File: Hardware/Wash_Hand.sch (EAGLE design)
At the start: 86 parts, among them IC1 LM358D, IC2 LP298XS, IC3 405016TSSOP, J1 I2C, J2 ICSP, J3 SPI, J4 9V_CONN, J5 EXT_VCC, J6 6_PIN_SERIAL_CABLEPTH, Q1 16.0 Mhz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

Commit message: Board/Schematic: CH340G; V3 goes to GND with 4.7-20nF..
while we also had VCC connected to it. That is the
datasheet says: "When using 5V operation, supply 5V
to VCC pin, and decouple the internal 3.3V reference with
a capacitor of 4.7-20nF from _V3 pin to ground_.

We had the VCC being hooked up to the capacitor..

Signed-off-by: Konrad Rzeszutek Wilk <konrad@kernel.org>
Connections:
- new net N$17: C14.1, JP6.1
- net VCC: no longer C14.1, JP6.1
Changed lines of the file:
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@@
 <label x="119.38" y="86.36" size="1.778" layer="95" rot="R180" xref="yes"/>
-</segment>
-<segment>
-<pinref part="C14" gate="G$1" pin="1"/>
-<wire x1="45.72" y1="96.52" x2="35.56" y2="96.52" width="0.1524" layer="91"/>
-<label x="35.56" y="96.52" size="1.778" layer="95" rot="R180" xref="yes"/>
-<pinref part="JP6" gate="G$1" pin="1"/>
-<wire x1="45.72" y1="96.52" x2="45.72" y2="99.06" width="0.1524" layer="91"/>
-<junction x="45.72" y="96.52"/>
 </segment>
 </net>
@@
 </segment>
 <segment>
+<pinref part="C16" gate="G$1" pin="1"/>
+<pinref part="X_36" gate="G$1" pin="0"/>
+<wire x1="121.92" y1="167.64" x2="121.92" y2="172.72" width="0.1524" layer="91"/>
+</segment>
+<segment>
 <pinref part="X_34" gate="G$1" pin="0"/>
 <pinref part="C14" gate="G$1" pin="2"/>
 <wire x1="45.72" y1="83.82" x2="45.72" y2="88.9" width="0.1524" layer="91"/>
-</segment>
-<segment>
-<pinref part="C16" gate="G$1" pin="1"/>
-<pinref part="X_36" gate="G$1" pin="0"/>
-<wire x1="121.92" y1="167.64" x2="121.92" y2="172.72" width="0.1524" layer="91"/>
 </segment>
 </net>
@@
 </segment>
 </net>
+<net name="N$17" class="0">
+<segment>
+<pinref part="C14" gate="G$1" pin="1"/>
+<pinref part="JP6" gate="G$1" pin="1"/>
+<wire x1="45.72" y1="96.52" x2="45.72" y2="99.06" width="0.1524" layer="91"/>
+</segment>
+</net>

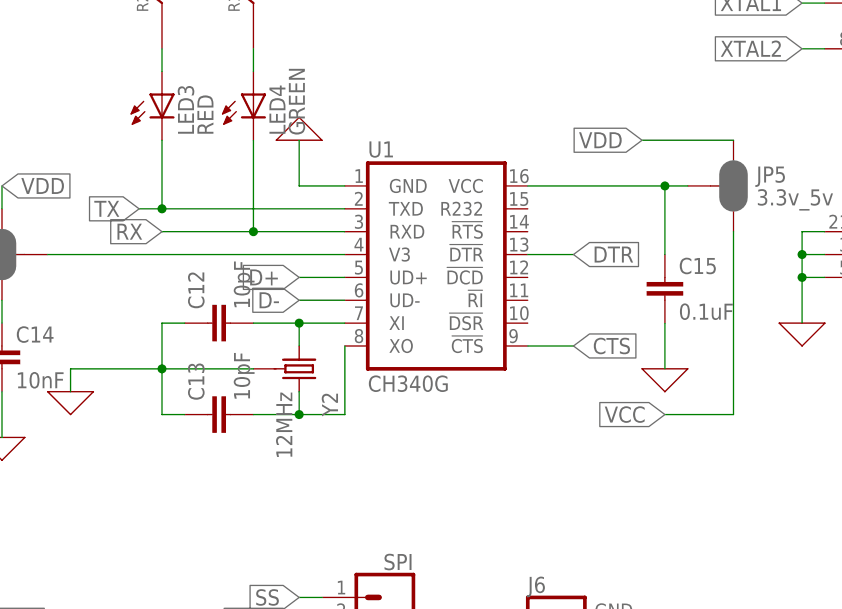
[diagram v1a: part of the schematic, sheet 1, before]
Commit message: Board/Schematic: Name the nets on the CH340G/Adjust location of GREEN,RED,CH340G
.. to make it easier to trace and diagnose.

Signed-off-by: Konrad Rzeszutek Wilk <konrad@kernel.org>
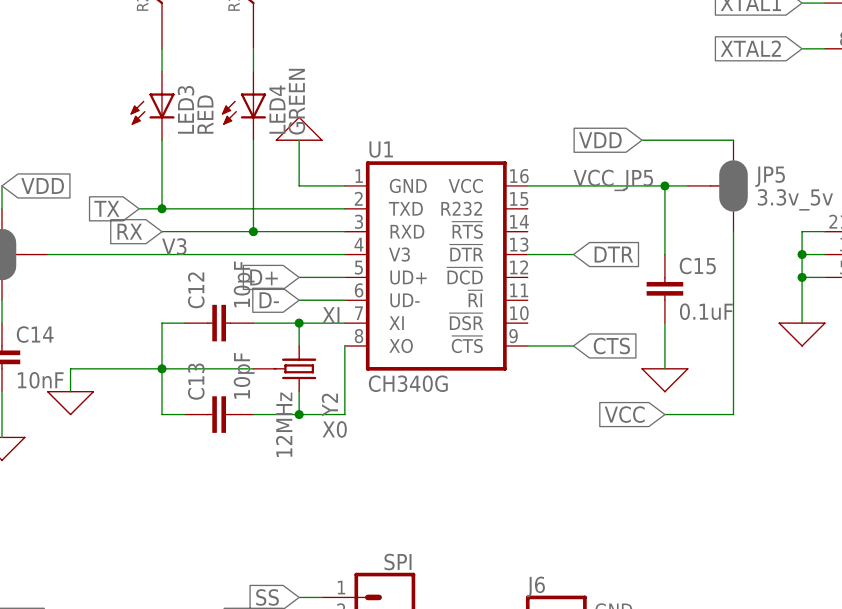
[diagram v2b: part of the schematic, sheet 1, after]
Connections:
- net N$1 renamed XI
- net N$19 renamed VCC_JP5
- net N$21 renamed X0
- net N$9 renamed V3
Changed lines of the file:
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@@
 </segment>
 </net>
-<net name="N$21" class="0">
+<net name="X0" class="0">
 <segment>
 <pinref part="U1" gate="U1" pin="XO"/>
@@
 <wire x1="73.66" y1="86.36" x2="78.74" y2="86.36" width="0.1524" layer="91"/>
 <junction x="78.74" y="86.36"/>
+<label x="81.28" y="83.82" size="1.778" layer="95"/>
 </segment>
 </net>
@@
 </segment>
 </net>
-<net name="N$1" class="0">
+<net name="XI" class="0">
 <segment>
 <pinref part="U1" gate="U1" pin="XI"/>
@@
 <wire x1="78.74" y1="96.52" x2="73.66" y2="96.52" width="0.1524" layer="91"/>
 <junction x="78.74" y="96.52"/>
+<label x="81.28" y="96.52" size="1.778" layer="95"/>
 </segment>
 </net>
@@
 </segment>
 </net>
-<net name="N$19" class="0">
+<net name="VCC_JP5" class="0">
 <segment>
 <pinref part="U1" gate="U1" pin="VCC"/>
@@
 <wire x1="119.38" y1="104.14" x2="119.38" y2="111.76" width="0.1524" layer="91"/>
 <junction x="119.38" y="111.76"/>
+<label x="109.22" y="111.76" size="1.778" layer="95"/>
 </segment>
 </net>
@@
 </segment>
 </net>
-<net name="N$9" class="0">
+<net name="V3" class="0">
 <segment>
 <pinref part="JP6" gate="G$1" pin="2"/>
 <pinref part="U1" gate="U1" pin="V3"/>
 <wire x1="50.8" y1="104.14" x2="83.82" y2="104.14" width="0.1524" layer="91"/>
+<label x="63.5" y="104.14" size="1.778" layer="95"/>
 </segment>
 </net>

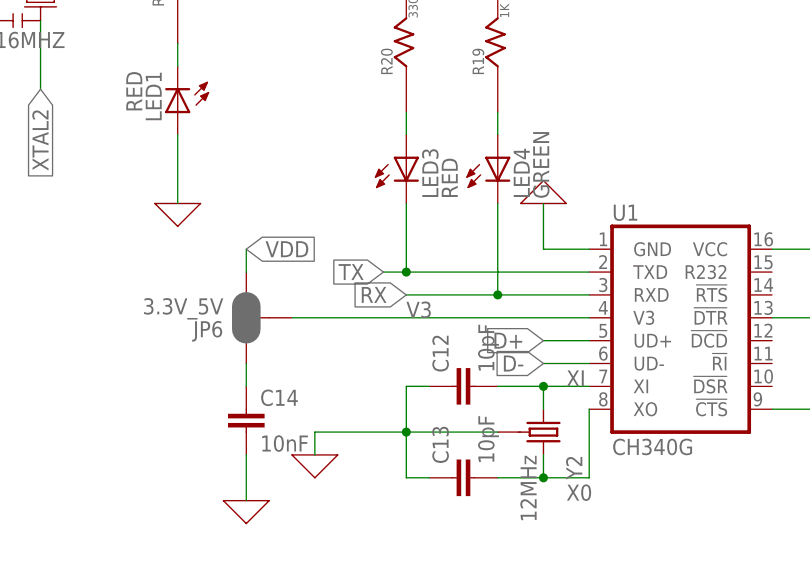
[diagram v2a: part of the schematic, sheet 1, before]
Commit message: Board/Schematic: Swap TX/RX on CH340G
.. as they are inversed.

Signed-off-by: Konrad Rzeszutek Wilk <konrad@kernel.org>
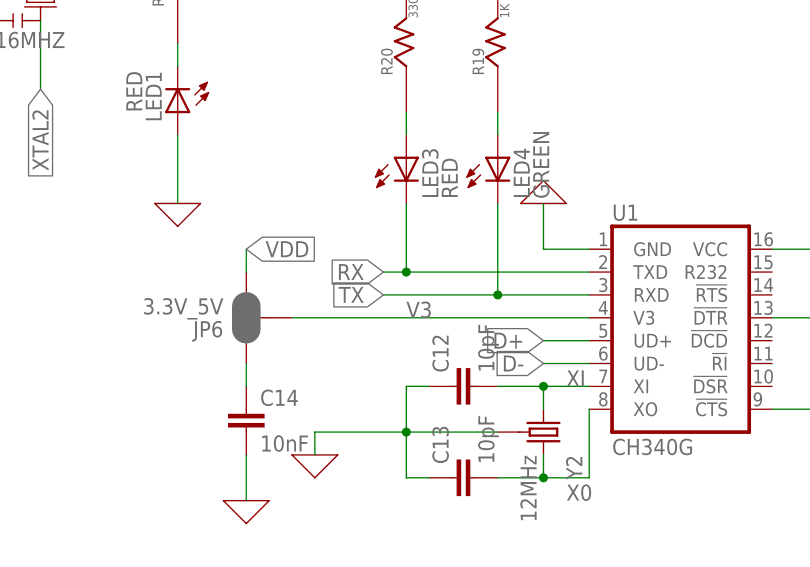
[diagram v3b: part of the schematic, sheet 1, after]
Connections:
- net RX: now also LED3.C, U1.TXD; no longer LED4.C, U1.RXD
- net TX: now also LED4.C, U1.RXD; no longer LED3.C, U1.TXD
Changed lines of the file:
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@@
 </segment>
 <segment>
-<pinref part="U1" gate="U1" pin="TXD"/>
-<wire x1="83.82" y1="109.22" x2="63.5" y2="109.22" width="0.1524" layer="91"/>
-<label x="60.96" y="109.22" size="1.778" layer="95" rot="R180" xref="yes"/>
-<pinref part="LED3" gate="G$1" pin="C"/>
-<wire x1="63.5" y1="109.22" x2="60.96" y2="109.22" width="0.1524" layer="91"/>
-<wire x1="63.5" y1="116.84" x2="63.5" y2="109.22" width="0.1524" layer="91"/>
-<junction x="63.5" y="109.22"/>
+<pinref part="U1" gate="U1" pin="RXD"/>
+<wire x1="83.82" y1="106.68" x2="73.66" y2="106.68" width="0.1524" layer="91"/>
+<pinref part="LED4" gate="G$1" pin="C"/>
+<wire x1="73.66" y1="106.68" x2="60.96" y2="106.68" width="0.1524" layer="91"/>
+<wire x1="73.66" y1="116.84" x2="73.66" y2="106.68" width="0.1524" layer="91"/>
+<junction x="73.66" y="106.68"/>
+<label x="60.96" y="106.68" size="1.778" layer="95" rot="R180" xref="yes"/>
 </segment>
 </net>
@@
 </segment>
 <segment>
-<pinref part="U1" gate="U1" pin="RXD"/>
-<wire x1="83.82" y1="106.68" x2="73.66" y2="106.68" width="0.1524" layer="91"/>
-<label x="63.5" y="106.68" size="1.778" layer="95" rot="R180" xref="yes"/>
-<pinref part="LED4" gate="G$1" pin="C"/>
-<wire x1="73.66" y1="106.68" x2="63.5" y2="106.68" width="0.1524" layer="91"/>
-<wire x1="73.66" y1="116.84" x2="73.66" y2="106.68" width="0.1524" layer="91"/>
-<junction x="73.66" y="106.68"/>
+<pinref part="U1" gate="U1" pin="TXD"/>
+<wire x1="83.82" y1="109.22" x2="63.5" y2="109.22" width="0.1524" layer="91"/>
+<pinref part="LED3" gate="G$1" pin="C"/>
+<wire x1="63.5" y1="109.22" x2="60.96" y2="109.22" width="0.1524" layer="91"/>
+<wire x1="63.5" y1="116.84" x2="63.5" y2="109.22" width="0.1524" layer="91"/>
+<junction x="63.5" y="109.22"/>
+<label x="60.96" y="109.22" size="1.778" layer="95" rot="R180" xref="yes"/>
 </segment>
 </net>

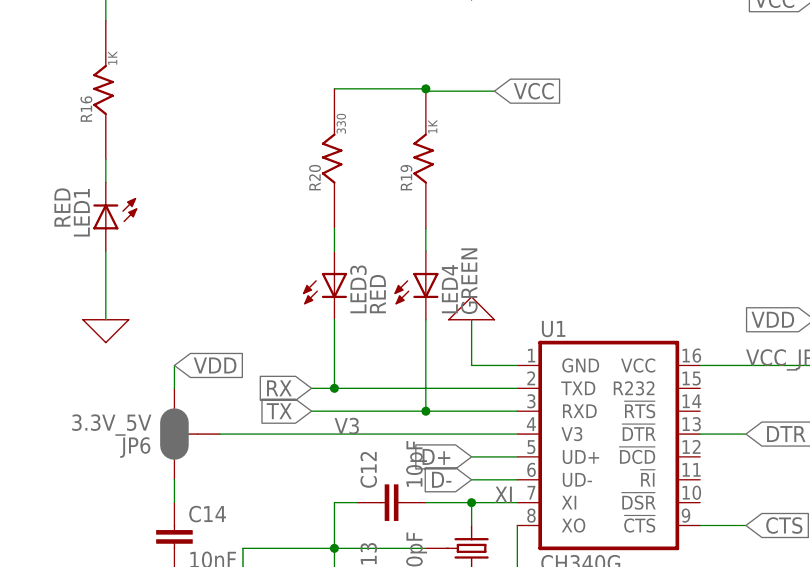
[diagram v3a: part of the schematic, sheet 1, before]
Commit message: Board/Schematic: s/LED3,LED4/TX,RX/
as it makes it much simpler to figure out on the board.

Signed-off-by: Konrad Rzeszutek Wilk <konrad@kernel.org>
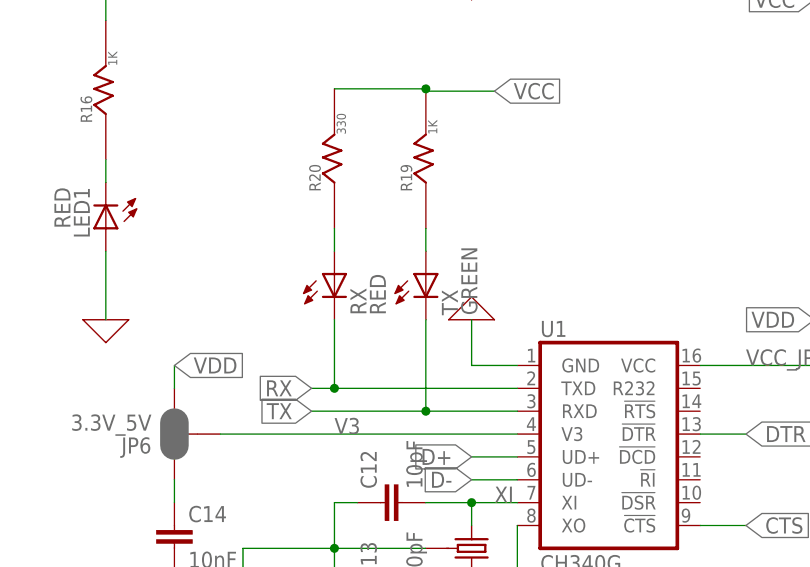
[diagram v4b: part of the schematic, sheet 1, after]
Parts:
- renumbered LED3 to RX, LED4 to TX
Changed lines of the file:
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@@
 <part name="R19" library="darnok_common" deviceset="RESISTOR" device="R1206" value="1K"/>
 <part name="R20" library="darnok_common" deviceset="RESISTOR" device="R1206" value="330"/>
-<part name="LED3" library="adafruit" library_urn="urn:adsk.eagle:library:420" deviceset="LED" device="SMT1206" package3d_urn="urn:adsk.eagle:package:6240349/1" value="RED"/>
-<part name="LED4" library="adafruit" library_urn="urn:adsk.eagle:library:420" deviceset="LED" device="SMT1206" package3d_urn="urn:adsk.eagle:package:6240349/1" value="GREEN"/>
+<part name="RX" library="adafruit" library_urn="urn:adsk.eagle:library:420" deviceset="LED" device="SMT1206" package3d_urn="urn:adsk.eagle:package:6240349/1" value="RED"/>
+<part name="TX" library="adafruit" library_urn="urn:adsk.eagle:library:420" deviceset="LED" device="SMT1206" package3d_urn="urn:adsk.eagle:package:6240349/1" value="GREEN"/>
 <part name="JP5" library="SparkFun-Jumpers" library_urn="urn:adsk.eagle:library:528" deviceset="JUMPER-SMT_3_2-NC_PASTE" device="_SILK" package3d_urn="urn:adsk.eagle:package:39294/1" value="3.3v_5v"/>
 <part name="JP6" library="SparkFun-Jumpers" library_urn="urn:adsk.eagle:library:528" deviceset="JUMPER-SMT_3_2-NC_PASTE" device="_SILK" package3d_urn="urn:adsk.eagle:package:39294/1" value="3.3V_5V"/>
@@
 <attribute name="VALUE" x="64.77" y="137.414" size="1.016" layer="96" rot="R90"/>
 </instance>
-<instance part="LED3" gate="G$1" x="63.5" y="121.92" smashed="yes">
+<instance part="RX" gate="G$1" x="63.5" y="121.92" smashed="yes">
 <attribute name="NAME" x="67.056" y="117.348" size="1.778" layer="95" rot="R90"/>
 <attribute name="VALUE" x="69.215" y="117.348" size="1.778" layer="96" rot="R90"/>
 </instance>
-<instance part="LED4" gate="G$1" x="73.66" y="121.92" smashed="yes">
+<instance part="TX" gate="G$1" x="73.66" y="121.92" smashed="yes">
 <attribute name="NAME" x="77.216" y="117.348" size="1.778" layer="95" rot="R90"/>
 <attribute name="VALUE" x="79.375" y="117.348" size="1.778" layer="96" rot="R90"/>
@@
 <pinref part="U1" gate="U1" pin="RXD"/>
 <wire x1="83.82" y1="106.68" x2="73.66" y2="106.68" width="0.1524" layer="91"/>
-<pinref part="LED4" gate="G$1" pin="C"/>
+<pinref part="TX" gate="G$1" pin="C"/>
 <wire x1="73.66" y1="106.68" x2="60.96" y2="106.68" width="0.1524" layer="91"/>
 <wire x1="73.66" y1="116.84" x2="73.66" y2="106.68" width="0.1524" layer="91"/>
@@
 <pinref part="U1" gate="U1" pin="TXD"/>
 <wire x1="83.82" y1="109.22" x2="63.5" y2="109.22" width="0.1524" layer="91"/>
-<pinref part="LED3" gate="G$1" pin="C"/>
+<pinref part="RX" gate="G$1" pin="C"/>
 <wire x1="63.5" y1="109.22" x2="60.96" y2="109.22" width="0.1524" layer="91"/>
 <wire x1="63.5" y1="116.84" x2="63.5" y2="109.22" width="0.1524" layer="91"/>
@@
 <net name="N$8" class="0">
 <segment>
-<pinref part="LED4" gate="G$1" pin="A"/>
+<pinref part="TX" gate="G$1" pin="A"/>
 <pinref part="R19" gate="G$1" pin="R_1"/>
 <wire x1="73.66" y1="124.46" x2="73.66" y2="127" width="0.1524" layer="91"/>
@@
 <net name="N$12" class="0">
 <segment>
-<pinref part="LED3" gate="G$1" pin="A"/>
+<pinref part="RX" gate="G$1" pin="A"/>
 <pinref part="R20" gate="G$1" pin="R_1"/>
 <wire x1="63.5" y1="124.46" x2="63.5" y2="127" width="0.1524" layer="91"/>
